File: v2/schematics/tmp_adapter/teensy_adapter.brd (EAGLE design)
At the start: 52.1 x 66.6 mm, 52 parts, among them IC1 TEENSY 3.6, IC2 ATMEGA1284P, J1 RADL, J2 I2C_2, J3 SPI_1, J4 Erw_analog, J5 I2C_0, J6 Erw_PWM, J7 Uart_5, J8 SPI_0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

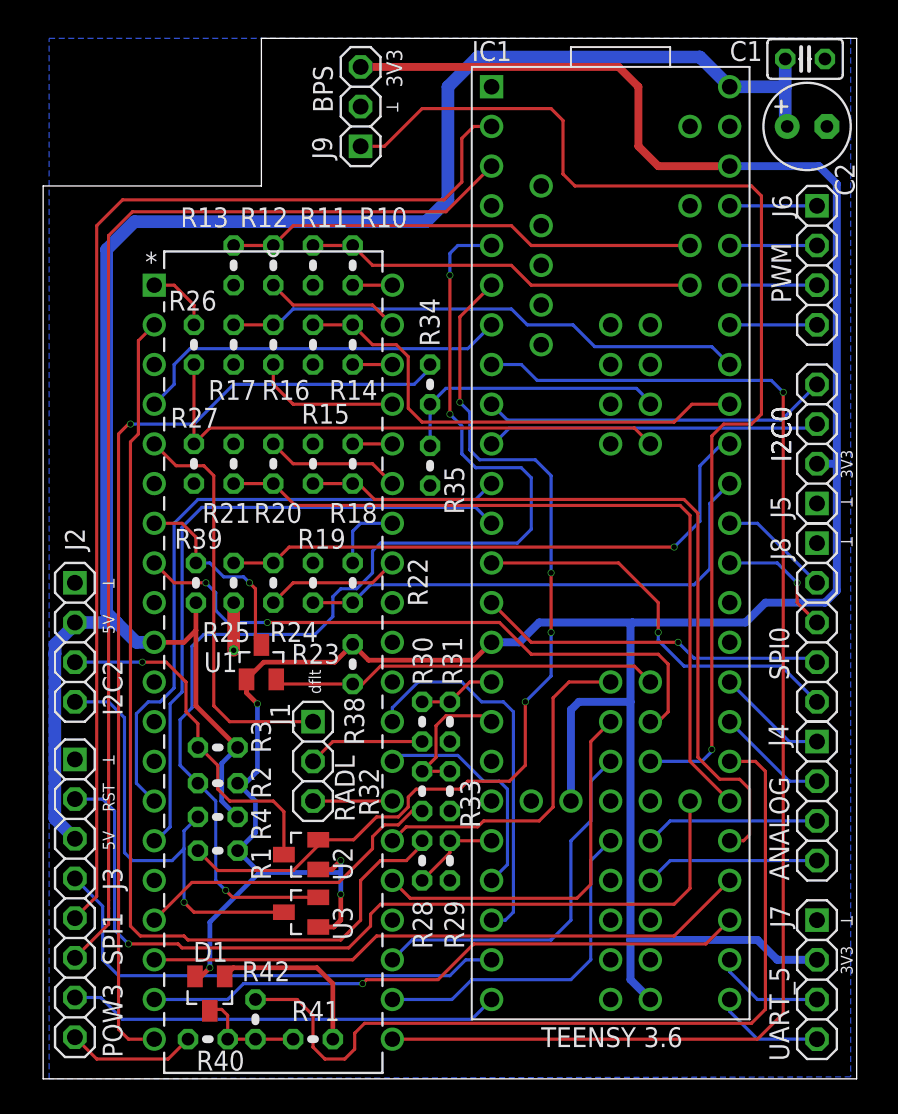
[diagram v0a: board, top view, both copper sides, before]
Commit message: bugfixes for wrong voltage dividers
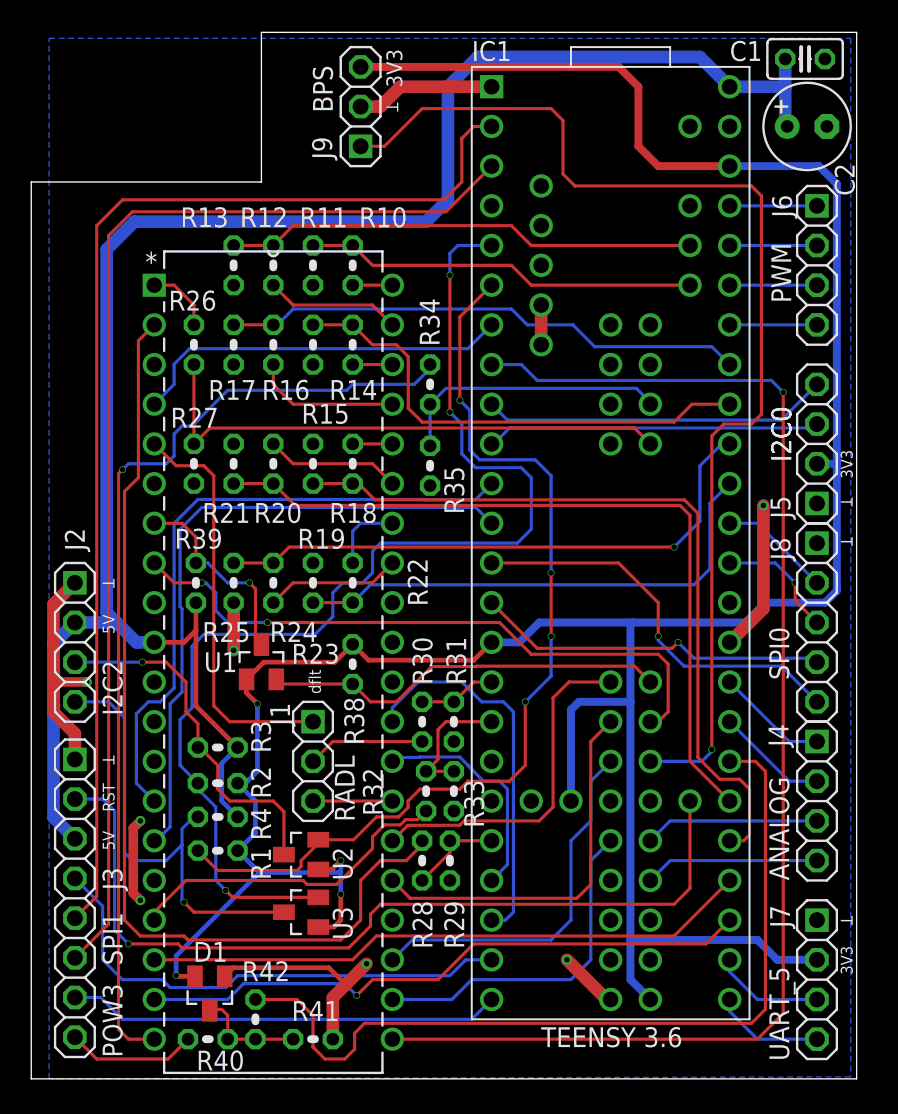
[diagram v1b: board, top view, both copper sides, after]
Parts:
- R14, R16, R18, R20, R22, R24, R28: value 2k2 -> 0
- R15, R17, R23, R25: value 3k9 -> 100k
- R19, R21: value 3k9 -> 820k
- R26, R34: value 2k2 -> 100k
- R27, R35: value 3k9 -> 180k
- R29: value 3k9 -> 47k
- moved R31 0.25 mm to (26.3, 22.9)
- moved R33 0.25 mm to (26.3, 18.4)
- moved R32 0.25 mm to (24.5, 18.4)
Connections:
- net SCL_5V renamed SCL2_5V
- net SDA_5V renamed SDA2_5V
- new net V_USB: IC1.VUSB
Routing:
- net GND: track 14.2 -> 62.2 mm, vias 1 -> 7
- net +3V3: track 187.0 -> 188.5 mm
- net MAUS_D_3V3: track 25.0 -> 25.9 mm
- net RADR: track 20.5 -> 21.2 mm
- net KLAPPE: track 62.6 -> 61.9 mm
- net RADR_3V3: track 9.04 -> 8.40 mm
- net MOT_L_PWM: track 38.9 -> 39.6 mm
- net CS1: track 31.7 -> 32.3 mm
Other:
- board size 52.1 x 66.6 mm -> 52.8 x 67 mm

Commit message: produced prototype version of adapter board
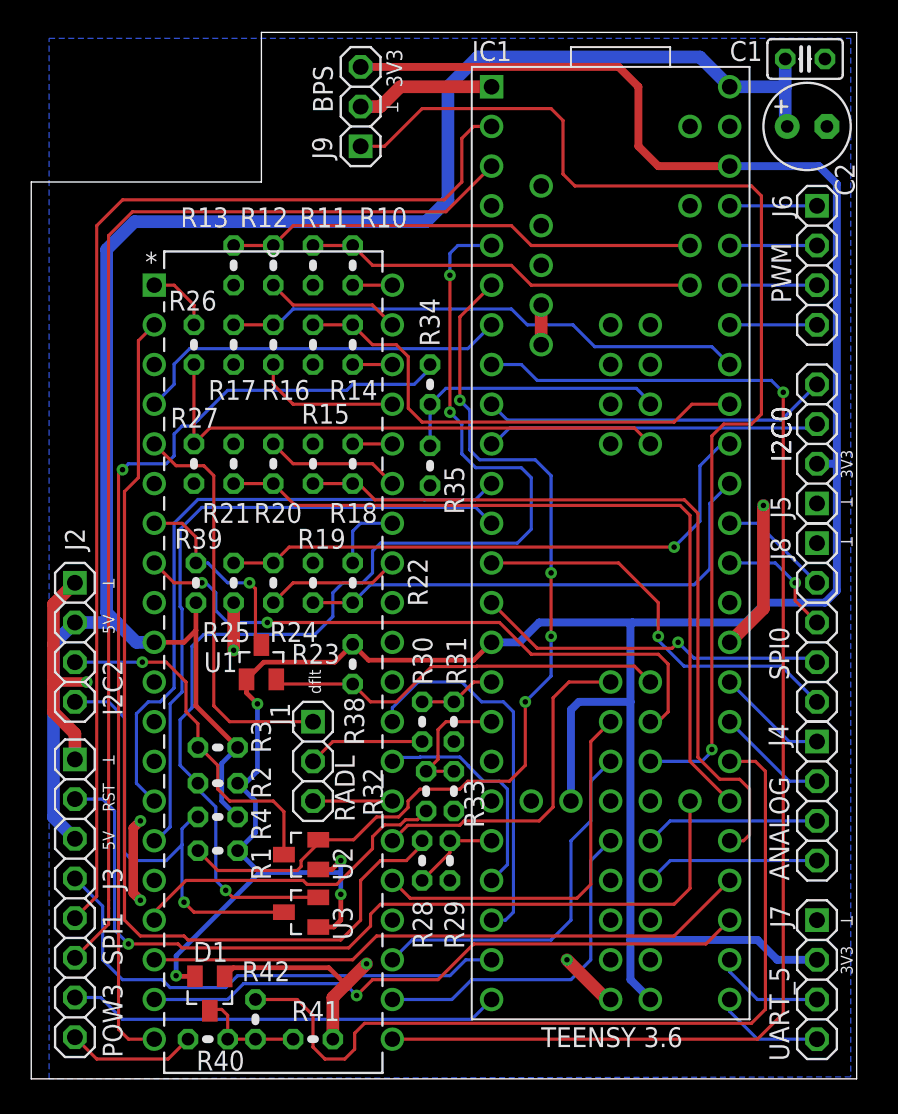
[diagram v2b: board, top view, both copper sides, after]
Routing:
- net SDA2: track 62.3 -> 61.6 mm
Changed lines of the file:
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@@
 <?xml version="1.0" encoding="utf-8"?>
 <!DOCTYPE eagle SYSTEM "eagle.dtd">
-<eagle version="9.0.1">
+<eagle version="9.1.0">
 <drawing>
 <settings>
@@
 </class>
 </classes>
-<designrules name="aisler_go_2layer_ts">
-<description language="de">&lt;b&gt;EAGLE Design Rules&lt;/b&gt;
-&lt;p&gt;
-Die Standard-Design-Rules sind so gewählt, dass sie für
-die meisten Anwendungen passen. Sollte ihre Platine
-besondere Anforderungen haben, treffen Sie die erforderlichen
-Einstellungen hier und speichern die Design Rules unter
-einem neuen Namen ab.</description>
-<description language="en">&lt;b&gt;EAGLE Design Rules&lt;/b&gt;
-&lt;p&gt;
-The default Design Rules have been set to cover
-a wide range of applications. Your particular design
-may have different requirements, so please make the
-necessary adjustments and save your customized
-design rules under a new name.</description>
+<designrules name="SeeedStudio_2layer_DRU">
+<description language="de">DRU for Seeed Fusion PCBs</description>
 <param name="layerSetup" value="(1*16)"/>
 <param name="mtCopper" value="0.035mm 0.035mm 0.035mm 0.035mm 0.035mm 0.035mm 0.035mm 0.035mm 0.035mm 0.035mm 0.035mm 0.035mm 0.035mm 0.035mm 0.035mm 0.035mm"/>
 <param name="mtIsolate" value="1.5mm 0.15mm 0.2mm 0.15mm 0.2mm 0.15mm 0.2mm 0.15mm 0.2mm 0.15mm 0.2mm 0.15mm 0.2mm 0.15mm 0.2mm"/>
-<param name="mdWireWire" value="0.12mm"/>
-<param name="mdWirePad" value="0.12mm"/>
-<param name="mdWireVia" value="0.12mm"/>
-<param name="mdPadPad" value="0.12mm"/>
-<param name="mdPadVia" value="0.12mm"/>
-<param name="mdViaVia" value="0.32mm"/>
-<param name="mdSmdPad" value="0.1mm"/>
-<param name="mdSmdVia" value="0.1mm"/>
-<param name="mdSmdSmd" value="0.1mm"/>
-<param name="mdViaViaSameLayer" value="8mil"/>
+<param name="mdWireWire" value="6mil"/>
+<param name="mdWirePad" value="6mil"/>
+<param name="mdWireVia" value="6mil"/>
+<param name="mdPadPad" value="6mil"/>
+<param name="mdPadVia" value="6mil"/>
+<param name="mdViaVia" value="6mil"/>
+<param name="mdSmdPad" value="6mil"/>
+<param name="mdSmdVia" value="6mil"/>
+<param name="mdSmdSmd" value="6mil"/>
+<param name="mdViaViaSameLayer" value="6mil"/>
 <param name="mnLayersViaInSmd" value="2"/>
-<param name="mdCopperDimension" value="0.3mm"/>
-<param name="mdDrill" value="0.3mm"/>
+<param name="mdCopperDimension" value="40mil"/>
+<param name="mdDrill" value="6mil"/>
 <param name="mdSmdStop" value="0mil"/>
-<param name="msWidth" value="0.15mm"/>
-<param name="msDrill" value="0.3mm"/>
-<param name="msMicroVia" value="0.1mm"/>
-<param name="msBlindViaRatio" value="1"/>
-<param name="rvPadTop" value="0.1"/>
-<param name="rvPadInner" value="0.1"/>
-<param name="rvPadBottom" value="0.1"/>
-<param name="rvViaOuter" value="0.1"/>
-<param name="rvViaInner" value="0.1"/>
-<param name="rvMicroViaOuter" value="0.1"/>
-<param name="rvMicroViaInner" value="0.1"/>
-<param name="rlMinPadTop" value="0.25mm"/>
-<param name="rlMaxPadTop" value="100mm"/>
-<param name="rlMinPadInner" value="0.25mm"/>
-<param name="rlMaxPadInner" value="100mm"/>
-<param name="rlMinPadBottom" value="0.25mm"/>
-<param name="rlMaxPadBottom" value="100mm"/>
-<param name="rlMinViaOuter" value="0.05mm"/>
-<param name="rlMaxViaOuter" value="100mm"/>
-<param name="rlMinViaInner" value="0.05mm"/>
-<param name="rlMaxViaInner" value="100mm"/>
-<param name="rlMinMicroViaOuter" value="0.05mm"/>
-<param name="rlMaxMicroViaOuter" value="100mm"/>
-<param name="rlMinMicroViaInner" value="0.05mm"/>
-<param name="rlMaxMicroViaInner" value="100mm"/>
+<param name="msWidth" value="6mil"/>
+<param name="msDrill" value="0.35mm"/>
+<param name="msMicroVia" value="9.99mm"/>
+<param name="msBlindViaRatio" value="0.5"/>
+<param name="rvPadTop" value="0.25"/>
+<param name="rvPadInner" value="0.25"/>
+<param name="rvPadBottom" value="0.25"/>
+<param name="rvViaOuter" value="0.25"/>
+<param name="rvViaInner" value="0.25"/>
+<param name="rvMicroViaOuter" value="0.25"/>
+<param name="rvMicroViaInner" value="0.25"/>
+<param name="rlMinPadTop" value="10mil"/>
+<param name="rlMaxPadTop" value="20mil"/>
+<param name="rlMinPadInner" value="10mil"/>
+<param name="rlMaxPadInner" value="20mil"/>
+<param name="rlMinPadBottom" value="10mil"/>
+<param name="rlMaxPadBottom" value="20mil"/>
+<param name="rlMinViaOuter" value="8mil"/>
+<param name="rlMaxViaOuter" value="20mil"/>
+<param name="rlMinViaInner" value="8mil"/>
+<param name="rlMaxViaInner" value="20mil"/>
+<param name="rlMinMicroViaOuter" value="4mil"/>
+<param name="rlMaxMicroViaOuter" value="20mil"/>
+<param name="rlMinMicroViaInner" value="4mil"/>
+<param name="rlMaxMicroViaInner" value="20mil"/>
 <param name="psTop" value="-1"/>
 <param name="psBottom" value="-1"/>
@@
 <param name="psElongationLong" value="100"/>
 <param name="psElongationOffset" value="100"/>
-<param name="mvStopFrame" value="0"/>
+<param name="mvStopFrame" value="1"/>
 <param name="mvCreamFrame" value="0"/>
-<param name="mlMinStopFrame" value="0.01mm"/>
-<param name="mlMaxStopFrame" value="100mm"/>
+<param name="mlMinStopFrame" value="4mil"/>
+<param name="mlMaxStopFrame" value="4mil"/>
 <param name="mlMinCreamFrame" value="0mil"/>
 <param name="mlMaxCreamFrame" value="0mil"/>
@@
 <param name="srRoundness" value="0"/>
 <param name="srMinRoundness" value="0mil"/>
-<param name="srMaxRoundness" value="100mm"/>
+<param name="srMaxRoundness" value="0mil"/>
 <param name="slThermalIsolate" value="10mil"/>
 <param name="slThermalsForVias" value="0"/>
@@
 <param name="checkRestrict" value="1"/>
 <param name="checkStop" value="0"/>
-<param name="checkValues" value="1"/>
+<param name="checkValues" value="0"/>
+<param name="checkNames" value="1"/>
+<param name="checkWireStubs" value="1"/>
+<param name="checkPolygonWidth" value="1"/>
 <param name="useDiameter" value="13"/>
-<param name="maxErrors" value="50"/>
+<param name="maxErrors" value="999999"/>
 </designrules>
 <autorouter>
@@
 <contactref element="U2" pad="S"/>
 <contactref element="R1" pad="1"/>
-<wire x1="17.417" y1="15.494" x2="17.61" y2="15.301" width="0.2032" layer="1"/>
 <wire x1="11.176" y1="13.335" x2="9.906" y2="14.605" width="0.2032" layer="1"/>
-<wire x1="17.61" y1="14.943" x2="17.61" y2="15.301" width="0.2032" layer="1"/>
 <wire x1="19.873" y1="15.301" x2="17.61" y2="15.301" width="0.2032" layer="1"/>
 <wire x1="32.512" y1="25.781" x2="32.512" y2="28.321" width="0.2032" layer="16"/>
@@
 </signal>
 </signals>
+<mfgpreviewcolors>
+<mfgpreviewcolor name="soldermaskcolor" color="0xC8008000"/>
+<mfgpreviewcolor name="silkscreencolor" color="0xFFFEFEFE"/>
+<mfgpreviewcolor name="backgroundcolor" color="0xFF282828"/>
+<mfgpreviewcolor name="coppercolor" color="0xFFFFBF00"/>
+<mfgpreviewcolor name="substratecolor" color="0xFF786E46"/>
+</mfgpreviewcolors>
 </board>
 </drawing>
